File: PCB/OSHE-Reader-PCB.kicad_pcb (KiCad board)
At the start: 4 copper layers, 117 x 100 mm, 99 parts, among them J1 2171750001, J2 112L-TDA0, J3 Conn_01x24_MountingPin, J4 S2B-PH-K-SLFSN, Q1 Q_PNP_BCEC, Q2 Si1308EDL, SW1 SW_Push, SW2 SW_Push, SW3 SW_Push, SW4 SW_Push, SW5 SW_Push, U1 BQ2057CSNTR, U2 IRF7326D2TRPBF, U3 TPS5432DDAR

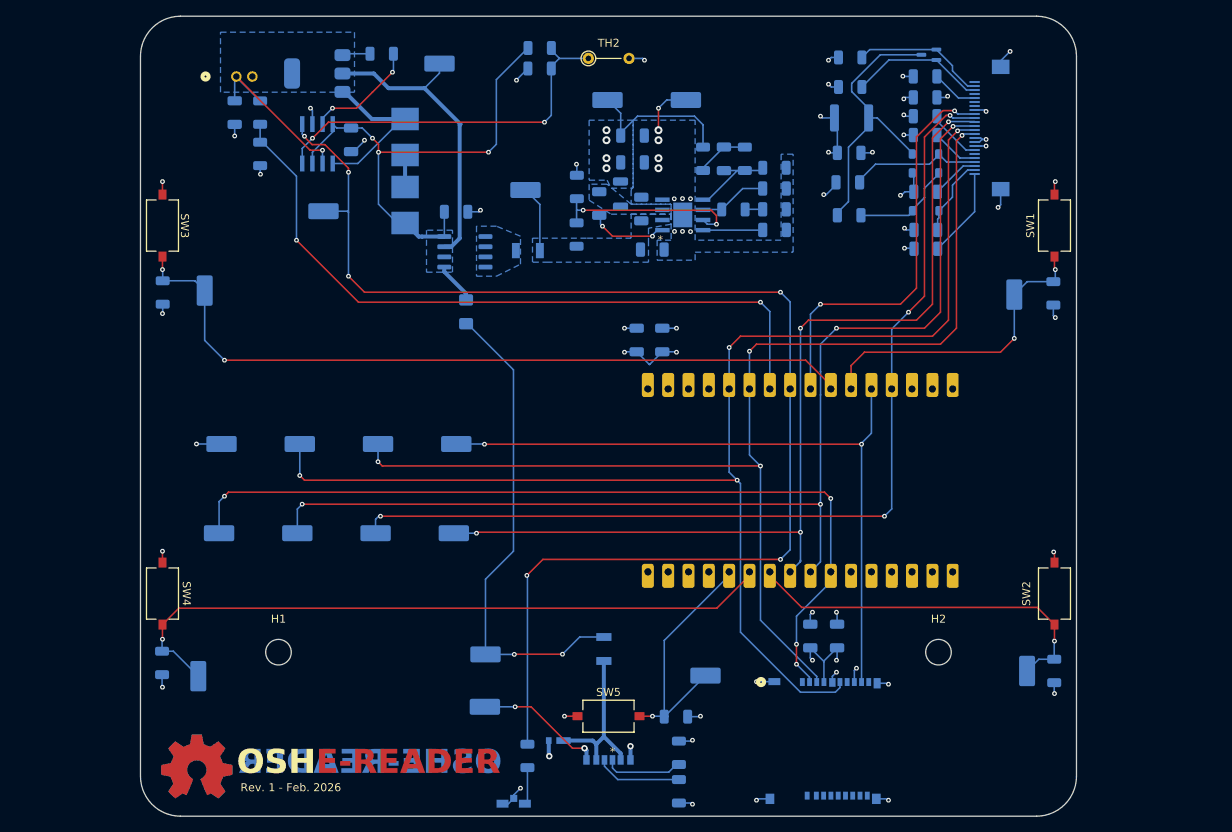
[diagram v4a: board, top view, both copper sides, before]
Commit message: Minor fixes to PCB: schottky diode for battery charging and general battery charging routing fixes
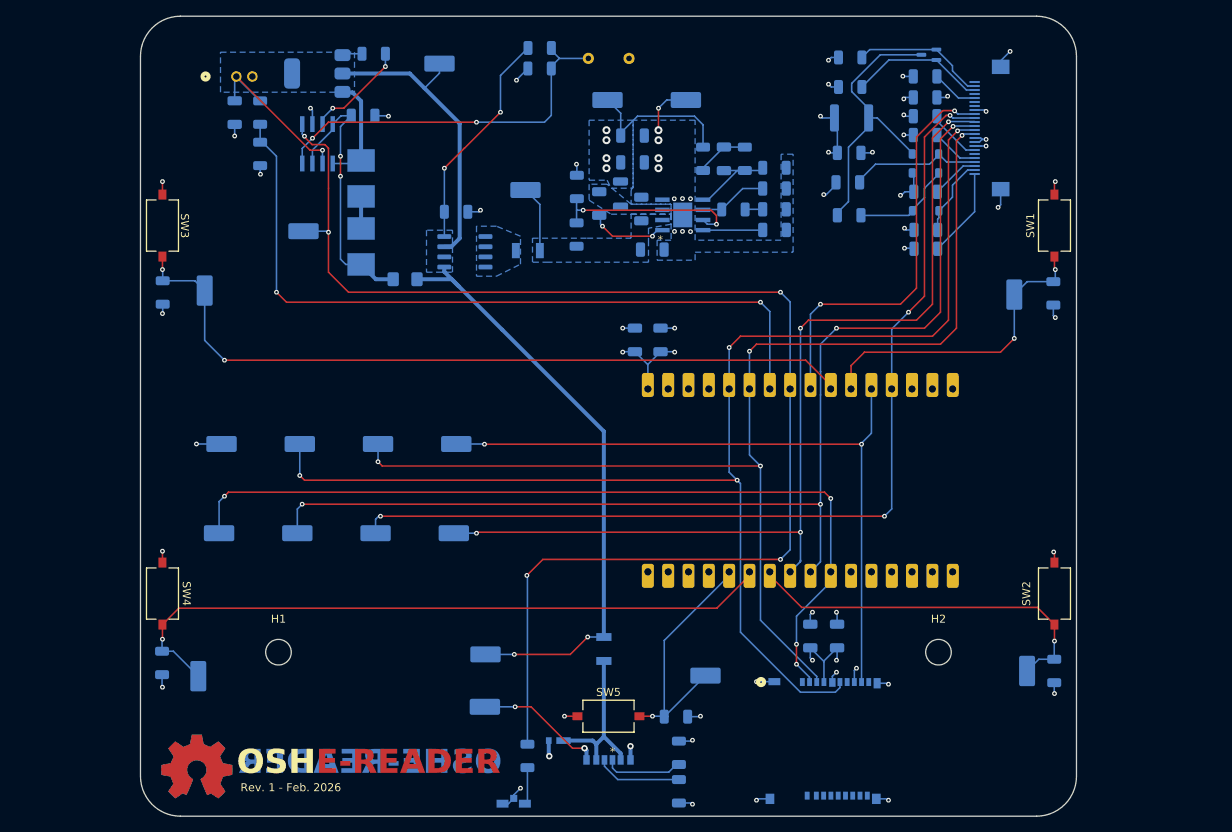
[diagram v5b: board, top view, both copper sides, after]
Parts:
- TH2: moved to B.Cu
- moved D4 8.64 mm to (64.6, 113.4), turned to 0 degrees
- moved R_{SNS}1 7.56 mm to (59.1, 109.3)
- moved R_{SNS}2 7.56 mm to (59.1, 100.8)
- moved TP_BAT_STAT1 3.54 mm to (51.9, 107.4)
- moved C1 3.35 mm to (59.3, 93.0), turned to 0 degrees
- moved R5 1.00 mm to (60.7, 85.2)
- moved C12 0.22 mm to (93.3, 121.0)
- moved C13 0.22 mm to (96.5, 121.0)
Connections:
- C1 pad 1: /Battery Charging/VBUS -> /Battery Charging/VBUS_PROT
- D4 pad 1: /Battery Charging/VBUS -> /Battery Charging/VBUS_PROT
- D4 pad 2: Net-(D4-A) -> /Battery Charging/VBUS
- F1 pad 2: Net-(D4-A) -> /Battery Charging/VBUS
- R_{SNS}1 pad 1: /Battery Charging/VBUS -> /Battery Charging/VBUS_PROT
- TP_VBUS1 pad 1: Net-(D4-A) -> /Battery Charging/VBUS
- U1 pad 3: /Battery Charging/VBUS -> /Battery Charging/VBUS_PROT
- U1 pad 8: /Battery Charging/VBUS -> /Battery Charging/VBUS_PROT
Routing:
- net Net-(D4-A): track 61.5 -> 0.00 mm, vias 2 -> 0
- net /Battery Charging/VBUS: track 67.9 -> 104.1 mm, vias 3 -> 4
- net /Battery Charging/VBUS_PROT: track 0.00 -> 35.1 mm, vias 0 -> 2
- net Net-(Q1-E): track 20.6 -> 13.9 mm
- net Net-(U4-GPIO0): track 89.1 -> 94.4 mm
- net +3V3: track 58.1 -> 61.1 mm
- net GND: track 100.9 -> 98.3 mm, vias 57 -> 56
- net Net-(U1-CC): track 14.2 -> 12.9 mm
- net /BAT_STAT: track 168.4 -> 169.6 mm, vias 6 -> 5
- net Net-(Q1-B): track 3.51 -> 2.51 mm
